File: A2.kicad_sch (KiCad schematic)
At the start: 143 parts, among them J1 Conn_Coaxial, J2 Conn_Coaxial, J3 Conn_Coaxial, J4 Conn_Coaxial, Q1 КТ315Г, Q2 КТ315Г, Q3 КТ361Г, Q4 КП307Г, Q5 КТ372В, U1 К155ТМ2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

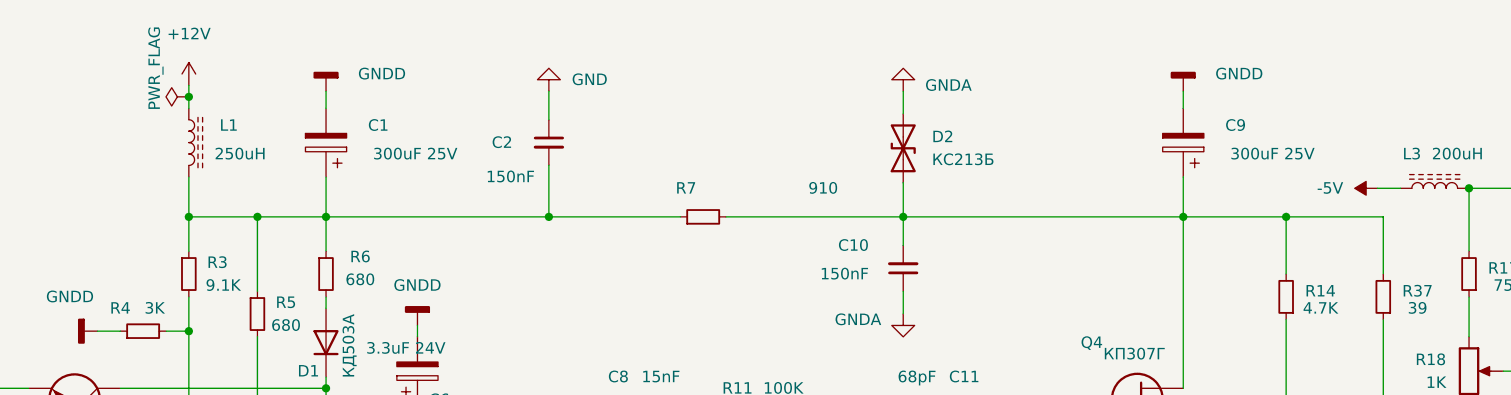
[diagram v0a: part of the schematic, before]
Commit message: A2: Adjust for ladihw symbols; fix voltages
Use ladihw library

Fix voltages:
 * -5.2V (ECL) is now used instead of -5V
 * 24V is now used instead of 12V
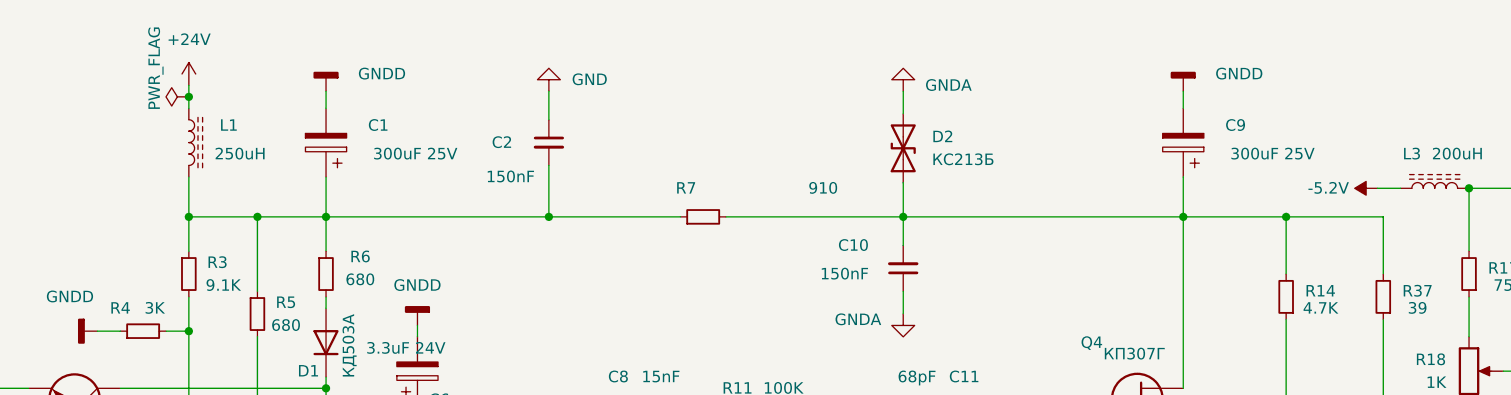
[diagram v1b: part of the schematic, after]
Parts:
- D1: symbol радио20:КД503А -> ladihw:КД503А
- D10, D9: symbol радио20:КД103А -> ladihw:КД103А
- D11, D12, D13, D14, D15, D16, D17, D18: symbol радио20:КА517А -> ladihw:КА517А
- Q1, Q2: symbol радио20:КТ315Г -> ladihw:КТ315Г
- Q3: symbol радио20:КТ361Г -> ladihw:КТ361Г
- Q4: symbol радио20:КП307Г -> ladihw:КП307Г
- Q5: symbol радио20:КТ372В -> ladihw:КТ372В
- U1: symbol радио20:К155ТМ2 -> ladihw:К155ТМ2
- U2: symbol радио20:К155ЛА3 -> ladihw:К155ЛА3
- U3: symbol радио20:К500ЛМ102 -> ladihw:К500ЛМ102
- W1, W2, W3, W4, W5, W6, W7, W8, W9: symbol радио20:Coaxial_Cable -> ladihw:Coaxial_Cable
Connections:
- net +12V renamed +24V
- new net: D18.1 (K), W8., W9.
- new net: D12.1 (K), W1., W3.
- new net: D16.1 (K), W6., W7.

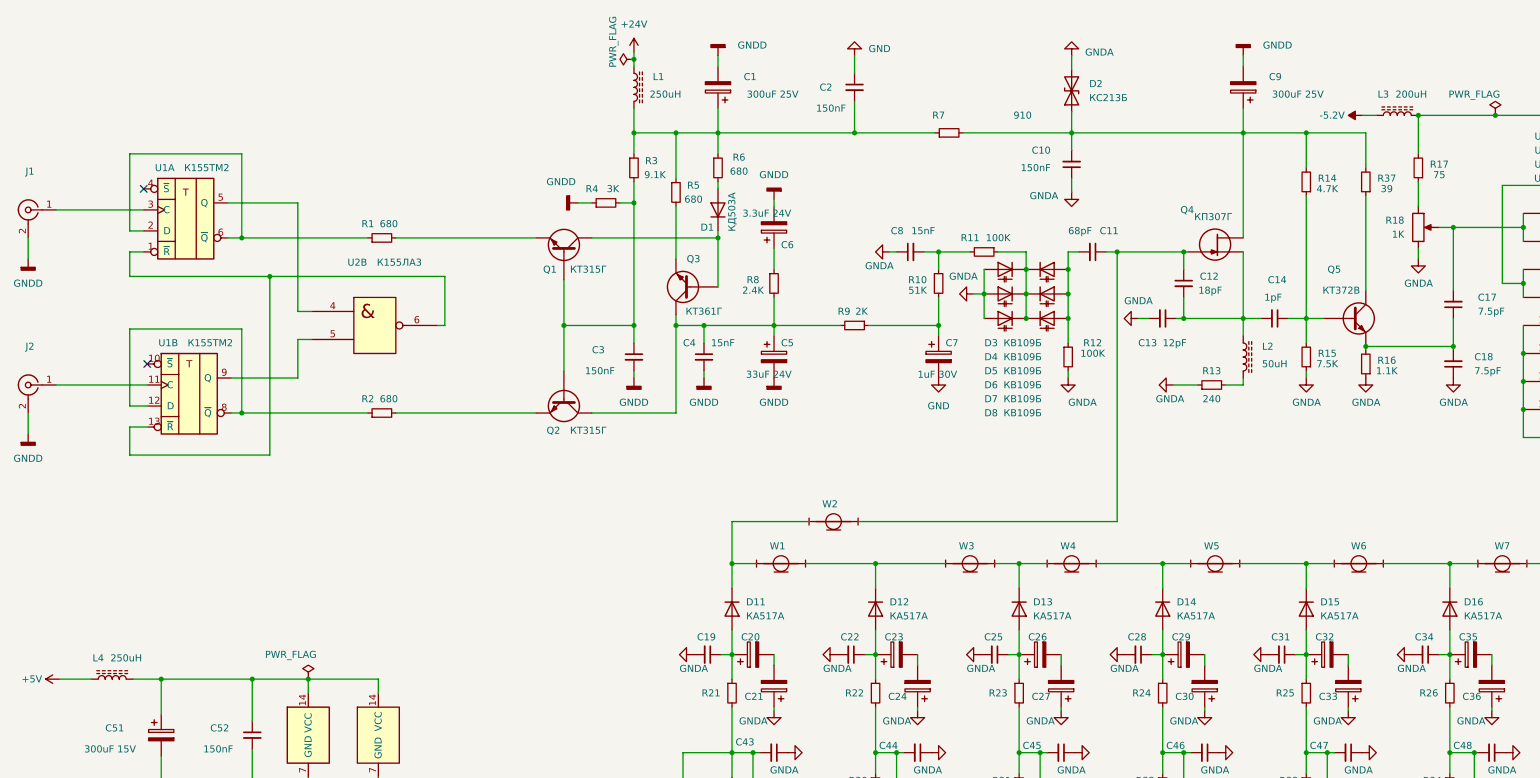
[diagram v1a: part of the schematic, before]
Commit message: Update to kicad7; flush WIP
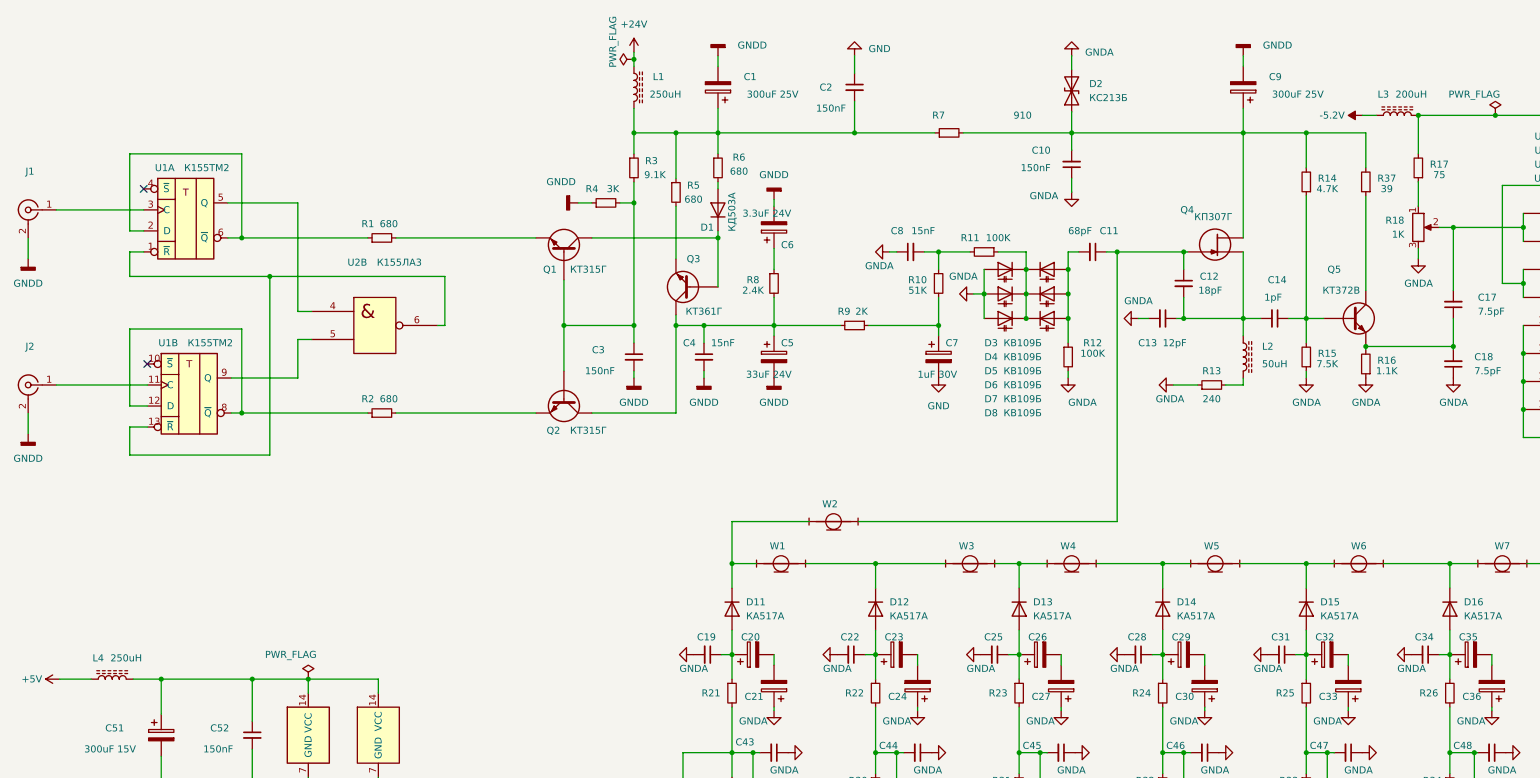
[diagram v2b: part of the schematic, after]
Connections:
- new net: D18.1 (K), W8., W9.
- new net: D12.1 (K), W1., W3.
- new net: D16.1 (K), W6., W7.

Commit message: Flush WIP
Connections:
- new net: D18.1 (K), W8., W9.
- new net: D12.1 (K), W1., W3.
- new net: D16.1 (K), W6., W7.
